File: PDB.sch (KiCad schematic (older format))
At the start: 3 parts

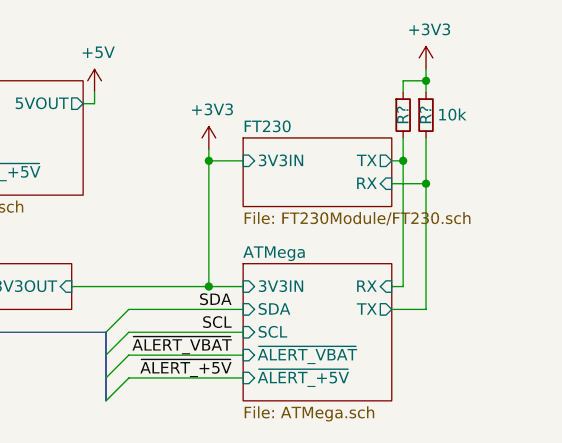
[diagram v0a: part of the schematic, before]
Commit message: add rx/tx labels
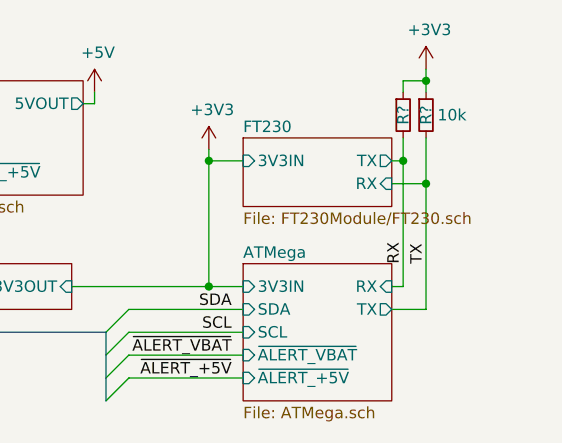
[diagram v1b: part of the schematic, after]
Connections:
- net ATMega/RX renamed RX
- net ATMega/TX renamed TX
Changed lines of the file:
@@
 Wire Wire Line
 	8700 2350 8700 2550
+Connection ~ 8700 2550
 Wire Bus Line
 	4300 2400 4300 2700
@@
 Wire Bus Line
 	7300 3200 7300 3500
-Connection ~ 8700 2550
+Text Label 8600 2900 1    50   ~ 0
+RX
+Text Label 8700 2900 1    50   ~ 0
+TX
 $EndSCHEMATC

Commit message: annotate parts
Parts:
- gave numbers to parts that had none: 3
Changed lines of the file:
@@
 P 3850 2250
 AR Path="/5C2F335D/5C33AF8D" Ref="C?"  Part="1"
-AR Path="/5C33AF8D" Ref="C?"  Part="1"
-F 0 "C?" H 3969 2525 50  0000 C CNN
+AR Path="/5C33AF8D" Ref="C1"  Part="1"
+F 0 "C1" H 3969 2525 50  0000 C CNN
 F 1 "XT-M" H 3969 2434 50  0000 C CNN
 F 2 "XT60:XT60PW" H 3850 2250 50  0001 C CNN
@@
 P 4000 2550
 AR Path="/5C2F335D/5C33AF94" Ref="#PWR?"  Part="1"
-AR Path="/5C33AF94" Ref="#PWR?"  Part="1"
-F 0 "#PWR?" H 4000 2300 50  0001 C CNN
+AR Path="/5C33AF94" Ref="#PWR01"  Part="1"
+F 0 "#PWR01" H 4000 2300 50  0001 C CNN
 F 1 "GND" H 4005 2377 50  0000 C CNN
 F 2 "" H 4000 2550 50  0001 C CNN
@@
 	3950 2200 4950 2200
 $Comp
-L power:+3V3 #PWR?
+L power:+3V3 #PWR03
 U 1 1 5C347B0C
 P 7750 2400
-F 0 "#PWR?" H 7750 2250 50  0001 C CNN
+F 0 "#PWR03" H 7750 2250 50  0001 C CNN
 F 1 "+3V3" H 7765 2573 50  0000 C CNN
 F 2 "" H 7750 2400 50  0001 C CNN
@@
 	7250 2200 7250 2150
 $Comp
-L power:+5V #PWR?
+L power:+5V #PWR02
 U 1 1 5C3483F6
 P 7250 2150
-F 0 "#PWR?" H 7250 2000 50  0001 C CNN
+F 0 "#PWR02" H 7250 2000 50  0001 C CNN
 F 1 "+5V" H 7265 2323 50  0000 C CNN
 F 2 "" H 7250 2150 50  0001 C CNN
@@
 	8700 3100 8550 3100
 $Comp
-L Device:R_Small R?
+L Device:R_Small R1
 U 1 1 5C32B264
 P 8600 2250
-F 0 "R?" V 8600 2250 50  0000 C CNN
+F 0 "R1" V 8600 2250 50  0000 C CNN
 F 1 "10k" H 8659 2205 50  0001 L CNN
 F 2 "Resistor_SMD:R_0603_1608Metric" H 8600 2250 50  0001 C CNN
@@
 $EndComp
 $Comp
-L Device:R_Small R?
+L Device:R_Small R2
 U 1 1 5C32B2AA
 P 8700 2250
-F 0 "R?" V 8700 2250 50  0000 C CNN
+F 0 "R2" V 8700 2250 50  0000 C CNN
 F 1 "10k" H 8750 2250 50  0000 L CNN
 F 2 "Resistor_SMD:R_0603_1608Metric" H 8700 2250 50  0001 C CNN
@@
 Connection ~ 8700 2100
 $Comp
-L power:+3V3 #PWR?
+L power:+3V3 #PWR04
 U 1 1 5C32C866
 P 8700 2050
-F 0 "#PWR?" H 8700 1900 50  0001 C CNN
+F 0 "#PWR04" H 8700 1900 50  0001 C CNN
 F 1 "+3V3" H 8715 2223 50  0000 C CNN
 F 2 "" H 8700 2050 50  0001 C CNN
@@
 	8700 2350 8700 2550
 Connection ~ 8700 2550
+Text Label 8600 2900 1    50   ~ 0
+RX
+Text Label 8700 2900 1    50   ~ 0
+TX
 Wire Bus Line
 	4300 2400 4300 2700
@@
 Wire Bus Line
 	7300 3200 7300 3500
-Text Label 8600 2900 1    50   ~ 0
-RX
-Text Label 8700 2900 1    50   ~ 0
-TX
 $EndSCHEMATC

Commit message: update XT60
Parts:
- C1: footprint XT60:XT60PW -> XT60:XT60PW-M
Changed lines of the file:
@@
 F 0 "C1" H 3969 2525 50  0000 C CNN
 F 1 "XT-M" H 3969 2434 50  0000 C CNN
-F 2 "XT60:XT60PW" H 3850 2250 50  0001 C CNN
+F 2 "XT60:XT60PW-M" H 3850 2250 50  0001 C CNN
 F 3 "" H 3850 2250 50  0001 C CNN
 	1    3850 2250

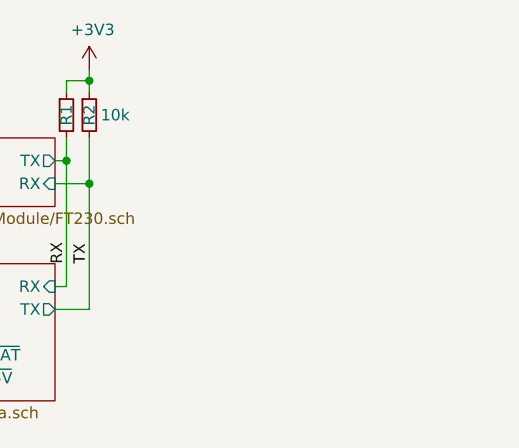
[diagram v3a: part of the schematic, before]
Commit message: add XT30 5V Out
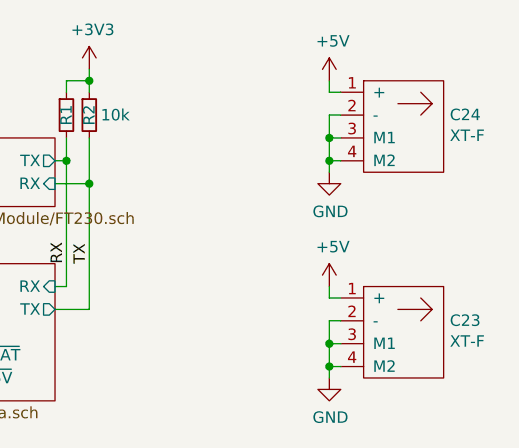
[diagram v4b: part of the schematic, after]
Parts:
- added C23, C24: XT-F, XT30:XT30PW-F, symbol amass:XT-F
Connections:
- net +5V: now also C23.1 (+), C24.1 (+)
- net GND: now also C23.2 (-), C23.3 (M1), C23.4 (M2), C24.2 (-), C24.3 (M1), C24.4 (M2)
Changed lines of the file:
@@
 F4 "3V3IN" I L 7900 2450 50
 $EndSheet
-Wire Wire Line
-	5850 2200 6550 2200
 Connection ~ 5850 2200
 Wire Wire Line
@@
 Text Label 8700 2900 1    50   ~ 0
 TX
+$Comp
+L amass:XT-F C23
+U 1 1 5C895801
+P 9900 3100
+F 0 "C23" H 10277 3051 50  0000 L CNN
+F 1 "XT-F" H 10277 2960 50  0000 L CNN
+F 2 "XT30:XT30PW-F" H 9900 3100 50  0001 C CNN
+F 3 "" H 9900 3100 50  0001 C CNN
+	1    9900 3100
+	1    0    0    -1
+$EndComp
+$Comp
+L power:+5V #PWR030
+U 1 1 5C8958C1
+P 9750 3000
+F 0 "#PWR030" H 9750 2850 50  0001 C CNN
+F 1 "+5V" H 9765 3173 50  0000 C CNN
+F 2 "" H 9750 3000 50  0001 C CNN
+F 3 "" H 9750 3000 50  0001 C CNN
+	1    9750 3000
+	1    0    0    -1
+$EndComp
+$Comp
+L power:GND #PWR?
+U 1 1 5C895918
+P 9750 3400
+AR Path="/5C2F335D/5C895918" Ref="#PWR?"  Part="1"
+AR Path="/5C895918" Ref="#PWR031"  Part="1"
+F 0 "#PWR031" H 9750 3150 50  0001 C CNN
+F 1 "GND" H 9755 3227 50  0000 C CNN
+F 2 "" H 9750 3400 50  0001 C CNN
+F 3 "" H 9750 3400 50  0001 C CNN
+	1    9750 3400
+	1    0    0    -1
+$EndComp
+Wire Wire Line
+	9750 3400 9750 3350
+Wire Wire Line
+	9750 3350 9800 3350
+Wire Wire Line
+	9750 3350 9750 3250
+Wire Wire Line
+	9750 3150 9800 3150
+Connection ~ 9750 3350
+Wire Wire Line
+	9800 3250 9750 3250
+Connection ~ 9750 3250
+Wire Wire Line
+	9750 3250 9750 3150
+Wire Wire Line
+	9800 3050 9750 3050
+Wire Wire Line
+	9750 3050 9750 3000
+$Comp
+L amass:XT-F C24
+U 1 1 5C899EE1
+P 9900 2200
+F 0 "C24" H 10277 2151 50  0000 L CNN
+F 1 "XT-F" H 10277 2060 50  0000 L CNN
+F 2 "XT30:XT30PW-F" H 9900 2200 50  0001 C CNN
+F 3 "" H 9900 2200 50  0001 C CNN
+	1    9900 2200
+	1    0    0    -1
+$EndComp
+$Comp
+L power:+5V #PWR032
+U 1 1 5C899EE7
+P 9750 2100
+F 0 "#PWR032" H 9750 1950 50  0001 C CNN
+F 1 "+5V" H 9765 2273 50  0000 C CNN
+F 2 "" H 9750 2100 50  0001 C CNN
+F 3 "" H 9750 2100 50  0001 C CNN
+	1    9750 2100
+	1    0    0    -1
+$EndComp
+$Comp
+L power:GND #PWR?
+U 1 1 5C899EED
+P 9750 2500
+AR Path="/5C2F335D/5C899EED" Ref="#PWR?"  Part="1"
+AR Path="/5C899EED" Ref="#PWR033"  Part="1"
+F 0 "#PWR033" H 9750 2250 50  0001 C CNN
+F 1 "GND" H 9755 2327 50  0000 C CNN
+F 2 "" H 9750 2500 50  0001 C CNN
+F 3 "" H 9750 2500 50  0001 C CNN
+	1    9750 2500
+	1    0    0    -1
+$EndComp
+Wire Wire Line
+	9750 2500 9750 2450
+Wire Wire Line
+	9750 2450 9800 2450
+Wire Wire Line
+	9750 2450 9750 2350
+Wire Wire Line
+	9750 2250 9800 2250
+Connection ~ 9750 2450
+Wire Wire Line
+	9800 2350 9750 2350
+Connection ~ 9750 2350
+Wire Wire Line
+	9750 2350 9750 2250
+Wire Wire Line
+	9800 2150 9750 2150
+Wire Wire Line
+	9750 2150 9750 2100
 Wire Bus Line
 	4300 2400 4300 2700
@@
 Wire Bus Line
 	7300 3200 7300 3500
+Wire Wire Line
+	5850 2200 6550 2200
 $EndSCHEMATC

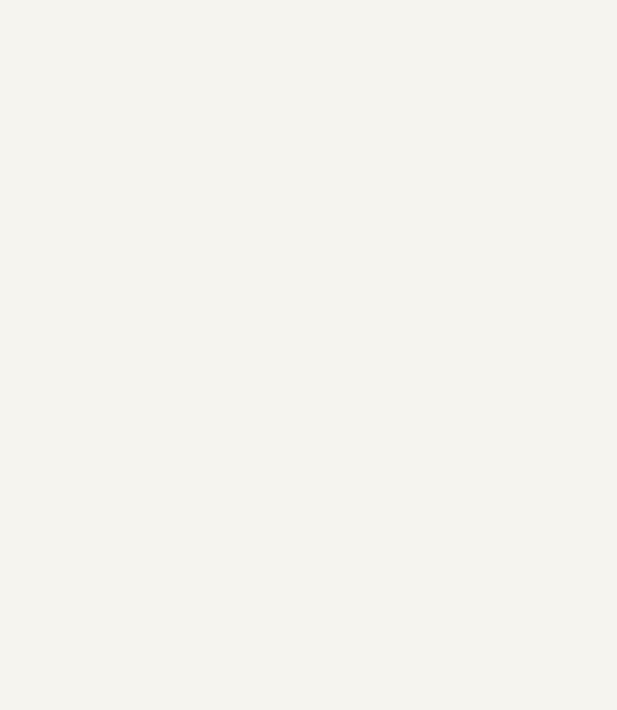
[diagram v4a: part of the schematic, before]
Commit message: USB C Power Port
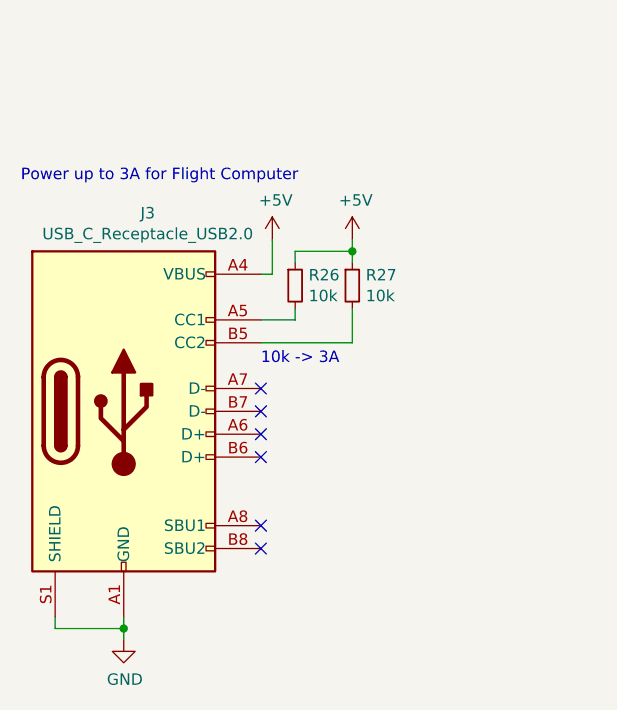
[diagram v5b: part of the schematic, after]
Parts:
- added J3: USB_C_Receptacle_USB2.0, GT-USB-7010:USB_C_Receptacle_GT-USB-7010, symbol Connector:USB_C_Receptacle_USB2.0
- added R26, R27: 10k, Resistor_SMD:R_0603_1608Metric, symbol Device:R_Small
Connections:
- net +5V: now also J3.A4 (VBUS), J3.A9 (VBUS), J3.B4 (VBUS), J3.B9 (VBUS), R26.1, R27.1
- net GND: now also J3.A1 (GND), J3.A12 (GND), J3.B1 (GND), J3.B12 (GND), J3.S1 (SHIELD)
- new net: J3.A5 (CC1), R26.2
- new net: J3.B5 (CC2), R27.2
- no-connect marks 0 -> 6
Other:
- note added: "10k -> 3A"
- note added: "Power up to 3A for Flight Computer"
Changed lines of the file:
@@
 Wire Wire Line
 	9750 2150 9750 2100
+Wire Wire Line
+	5850 2200 6550 2200
+$Comp
+L Connector:USB_C_Receptacle_USB2.0 J3
+U 1 1 5C8A8E22
+P 2200 4950
+F 0 "J3" H 2305 5817 50  0000 C CNN
+F 1 "USB_C_Receptacle_USB2.0" H 2305 5726 50  0000 C CNN
+F 2 "GT-USB-7010:USB_C_Receptacle_GT-USB-7010" H 2350 4950 50  0001 C CNN
+F 3 "https://www.usb.org/sites/default/files/documents/usb_type-c.zip" H 2350 4950 50  0001 C CNN
+	1    2200 4950
+	1    0    0    -1
+$EndComp
+$Comp
+L power:+5V #PWR035
+U 1 1 5C8A9251
+P 2850 4200
+F 0 "#PWR035" H 2850 4050 50  0001 C CNN
+F 1 "+5V" H 2865 4373 50  0000 C CNN
+F 2 "" H 2850 4200 50  0001 C CNN
+F 3 "" H 2850 4200 50  0001 C CNN
+	1    2850 4200
+	1    0    0    -1
+$EndComp
+Wire Wire Line
+	2850 4350 2800 4350
+$Comp
+L Device:R_Small R26
+U 1 1 5C8AB34A
+P 2950 4400
+F 0 "R26" H 3009 4446 50  0000 L CNN
+F 1 "10k" H 3009 4355 50  0000 L CNN
+F 2 "Resistor_SMD:R_0603_1608Metric" H 2950 4400 50  0001 C CNN
+F 3 "~" H 2950 4400 50  0001 C CNN
+	1    2950 4400
+	1    0    0    -1
+$EndComp
+$Comp
+L Device:R_Small R27
+U 1 1 5C8AB496
+P 3200 4400
+F 0 "R27" H 3259 4446 50  0000 L CNN
+F 1 "10k" H 3259 4355 50  0000 L CNN
+F 2 "Resistor_SMD:R_0603_1608Metric" H 3200 4400 50  0001 C CNN
+F 3 "~" H 3200 4400 50  0001 C CNN
+	1    3200 4400
+	1    0    0    -1
+$EndComp
+Wire Wire Line
+	2800 4550 2950 4550
+Wire Wire Line
+	2950 4550 2950 4500
+Wire Wire Line
+	2800 4650 3200 4650
+Wire Wire Line
+	3200 4650 3200 4500
+Wire Wire Line
+	2950 4300 2950 4250
+Wire Wire Line
+	3200 4300 3200 4250
+Wire Wire Line
+	3200 4250 2950 4250
+Wire Wire Line
+	2850 4200 2850 4350
+Wire Wire Line
+	3200 4250 3200 4200
+Connection ~ 3200 4250
+$Comp
+L power:+5V #PWR036
+U 1 1 5C8B41F2
+P 3200 4200
+F 0 "#PWR036" H 3200 4050 50  0001 C CNN
+F 1 "+5V" H 3215 4373 50  0000 C CNN
+F 2 "" H 3200 4200 50  0001 C CNN
+F 3 "" H 3200 4200 50  0001 C CNN
+	1    3200 4200
+	1    0    0    -1
+$EndComp
+Text Notes 2800 4750 0    50   ~ 0
+10k -> 3A
+NoConn ~ 2800 4850
+NoConn ~ 2800 4950
+NoConn ~ 2800 5050
+NoConn ~ 2800 5150
+NoConn ~ 2800 5450
+NoConn ~ 2800 5550
+$Comp
+L power:GND #PWR?
+U 1 1 5C8BB2AE
+P 2200 5950
+AR Path="/5C2F335D/5C8BB2AE" Ref="#PWR?"  Part="1"
+AR Path="/5C8BB2AE" Ref="#PWR034"  Part="1"
+F 0 "#PWR034" H 2200 5700 50  0001 C CNN
+F 1 "GND" H 2205 5777 50  0000 C CNN
+F 2 "" H 2200 5950 50  0001 C CNN
+F 3 "" H 2200 5950 50  0001 C CNN
+	1    2200 5950
+	1    0    0    -1
+$EndComp
+Wire Wire Line
+	1900 5850 1900 5900
+Wire Wire Line
+	1900 5900 2200 5900
+Wire Wire Line
+	2200 5900 2200 5850
+Wire Wire Line
+	2200 5950 2200 5900
 Wire Bus Line
 	4300 2400 4300 2700
@@
 Wire Bus Line
 	7300 3200 7300 3500
-Wire Wire Line
-	5850 2200 6550 2200
+Connection ~ 2200 5900
+Text Notes 1750 3950 0    50   ~ 0
+Power up to 3A for Flight Computer
 $EndSCHEMATC

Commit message: wip und so
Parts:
- removed C1: XT-M, XT60:XT60PW-M, symbol amass:XT-M
- removed C23, C24: XT-F, XT30:XT30PW-F, symbol amass:XT-F
- removed J3: USB_C_Receptacle_USB2.0, GT-USB-7010:USB_C_Receptacle_GT-USB-7010, symbol Connector:USB_C_Receptacle_USB2.0
- removed R26, R27: 10k, Resistor_SMD:R_0603_1608Metric, symbol Device:R_Small
- added J3, J4, J5: Conn_01x02, XT30:XT30PB-F, symbol Connector_Generic:Conn_01x02
- added J6: Conn_01x02, XT60:XT60PB-M, symbol Connector_Generic:Conn_01x02
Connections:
- net +5V: now also J3.2 (Pin_2), J4.2 (Pin_2), J5.2 (Pin_2)
- net BAT/VBATIN: now also J6.2 (Pin_2)
- net GND: now also J3.1 (Pin_1), J4.1 (Pin_1), J5.1 (Pin_1), J6.1 (Pin_1)
- no-connect marks 6 -> 0
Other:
- note removed: "10k -> 3A"
- note removed: "Power up to 3A for Flight Computer"

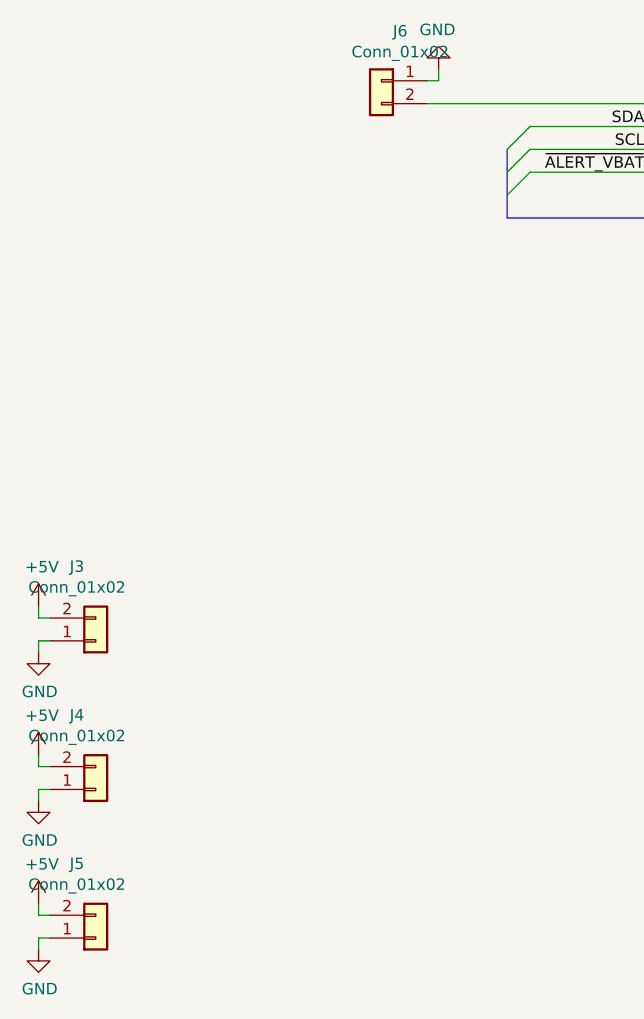
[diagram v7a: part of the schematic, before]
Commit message: LMZM23600 from kicad libs
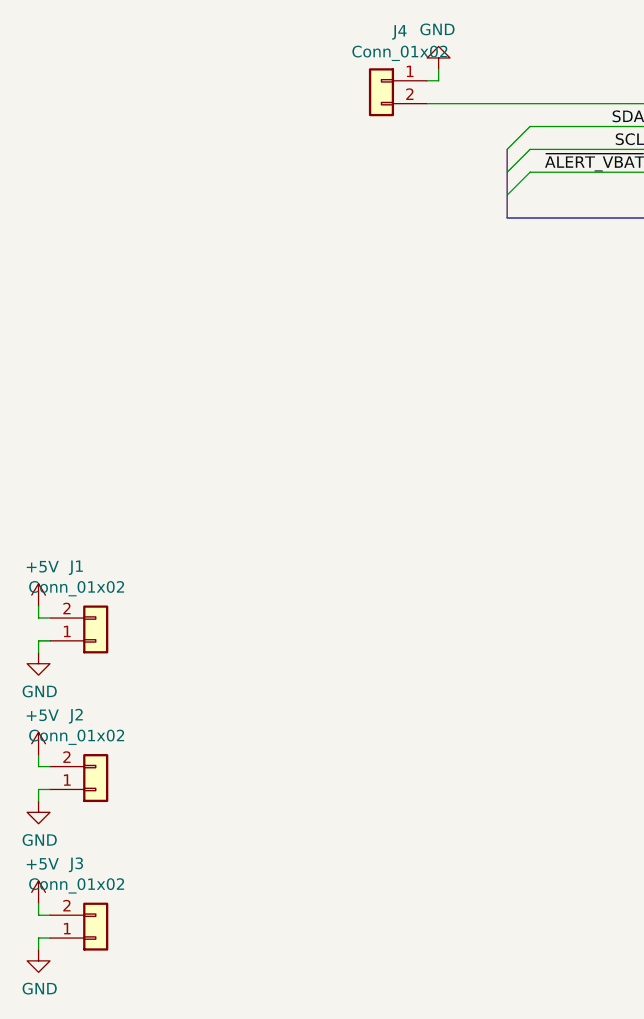
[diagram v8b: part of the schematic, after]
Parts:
- renumbered J3 to J1, J4 to J2, J5 to J3, J6 to J4
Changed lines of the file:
@@
 P 4000 2050
 AR Path="/5C2F335D/5C33AF94" Ref="#PWR?"  Part="1"
-AR Path="/5C33AF94" Ref="#PWR01"  Part="1"
-F 0 "#PWR01" H 4000 1800 50  0001 C CNN
+AR Path="/5C33AF94" Ref="#PWR07"  Part="1"
+F 0 "#PWR07" H 4000 1800 50  0001 C CNN
 F 1 "GND" H 4005 1877 50  0000 C CNN
 F 2 "" H 4000 2050 50  0001 C CNN
@@
 	3950 2200 4950 2200
 $Comp
-L power:+3V3 #PWR03
+L power:+3V3 #PWR09
 U 1 1 5C347B0C
 P 7750 2400
-F 0 "#PWR03" H 7750 2250 50  0001 C CNN
+F 0 "#PWR09" H 7750 2250 50  0001 C CNN
 F 1 "+3V3" H 7765 2573 50  0000 C CNN
 F 2 "" H 7750 2400 50  0001 C CNN
@@
 	7250 2200 7250 2150
 $Comp
-L power:+5V #PWR02
+L power:+5V #PWR08
 U 1 1 5C3483F6
 P 7250 2150
-F 0 "#PWR02" H 7250 2000 50  0001 C CNN
+F 0 "#PWR08" H 7250 2000 50  0001 C CNN
 F 1 "+5V" H 7265 2323 50  0000 C CNN
 F 2 "" H 7250 2150 50  0001 C CNN
@@
 Connection ~ 8700 2100
 $Comp
-L power:+3V3 #PWR04
+L power:+3V3 #PWR010
 U 1 1 5C32C866
 P 8700 2050
-F 0 "#PWR04" H 8700 1900 50  0001 C CNN
+F 0 "#PWR010" H 8700 1900 50  0001 C CNN
 F 1 "+3V3" H 8715 2223 50  0000 C CNN
 F 2 "" H 8700 2050 50  0001 C CNN
@@
 TX
 $Comp
-L power:+5V #PWR030
+L power:+5V #PWR03
 U 1 1 5C8958C1
 P 2250 5050
-F 0 "#PWR030" H 2250 4900 50  0001 C CNN
+F 0 "#PWR03" H 2250 4900 50  0001 C CNN
 F 1 "+5V" H 2265 5223 50  0000 C CNN
 F 2 "" H 2250 5050 50  0001 C CNN
@@
 P 2250 5250
 AR Path="/5C2F335D/5C895918" Ref="#PWR?"  Part="1"
-AR Path="/5C895918" Ref="#PWR031"  Part="1"
-F 0 "#PWR031" H 2250 5000 50  0001 C CNN
+AR Path="/5C895918" Ref="#PWR04"  Part="1"
+F 0 "#PWR04" H 2250 5000 50  0001 C CNN
 F 1 "GND" H 2255 5077 50  0000 C CNN
 F 2 "" H 2250 5250 50  0001 C CNN
@@
 	2250 5100 2250 5050
 $Comp
-L power:+5V #PWR032
+L power:+5V #PWR01
 U 1 1 5C899EE7
 P 2250 4400
-F 0 "#PWR032" H 2250 4250 50  0001 C CNN
+F 0 "#PWR01" H 2250 4250 50  0001 C CNN
 F 1 "+5V" H 2265 4573 50  0000 C CNN
 F 2 "" H 2250 4400 50  0001 C CNN
@@
 P 2250 4600
 AR Path="/5C2F335D/5C899EED" Ref="#PWR?"  Part="1"
-AR Path="/5C899EED" Ref="#PWR033"  Part="1"
-F 0 "#PWR033" H 2250 4350 50  0001 C CNN
+AR Path="/5C899EED" Ref="#PWR02"  Part="1"
+F 0 "#PWR02" H 2250 4350 50  0001 C CNN
 F 1 "GND" H 2255 4427 50  0000 C CNN
 F 2 "" H 2250 4600 50  0001 C CNN
@@
 	5850 2200 6550 2200
 $Comp
-L Connector_Generic:Conn_01x02 J4
+L Connector_Generic:Conn_01x02 J2
 U 1 1 5CAA71D1
 P 2500 5200
-F 0 "J4" H 2418 4875 50  0000 C CNN
+F 0 "J2" H 2418 4875 50  0000 C CNN
 F 1 "Conn_01x02" H 2418 4966 50  0000 C CNN
 F 2 "XT30:XT30PB-F" H 2500 5200 50  0001 C CNN
@@
 	2250 5200 2250 5250
 $Comp
-L Connector_Generic:Conn_01x02 J3
+L Connector_Generic:Conn_01x02 J1
 U 1 1 5CAA665E
 P 2500 4550
-F 0 "J3" H 2418 4225 50  0000 C CNN
+F 0 "J1" H 2418 4225 50  0000 C CNN
 F 1 "Conn_01x02" H 2418 4316 50  0000 C CNN
 F 2 "XT30:XT30PB-F" H 2500 4550 50  0001 C CNN
@@
 	2250 4600 2250 4550
 $Comp
-L power:+5V #PWR0101
+L power:+5V #PWR05
 U 1 1 5CAABE9B
 P 2250 5700
-F 0 "#PWR0101" H 2250 5550 50  0001 C CNN
+F 0 "#PWR05" H 2250 5550 50  0001 C CNN
 F 1 "+5V" H 2265 5873 50  0000 C CNN
 F 2 "" H 2250 5700 50  0001 C CNN
@@
 P 2250 5900
 AR Path="/5C2F335D/5CAABEA5" Ref="#PWR?"  Part="1"
-AR Path="/5CAABEA5" Ref="#PWR0102"  Part="1"
-F 0 "#PWR0102" H 2250 5650 50  0001 C CNN
+AR Path="/5CAABEA5" Ref="#PWR06"  Part="1"
+F 0 "#PWR06" H 2250 5650 50  0001 C CNN
 F 1 "GND" H 2255 5727 50  0000 C CNN
 F 2 "" H 2250 5900 50  0001 C CNN
@@
 	2250 5750 2250 5700
 $Comp
-L Connector_Generic:Conn_01x02 J5
+L Connector_Generic:Conn_01x02 J3
 U 1 1 5CAABEB2
 P 2500 5850
-F 0 "J5" H 2418 5525 50  0000 C CNN
+F 0 "J3" H 2418 5525 50  0000 C CNN
 F 1 "Conn_01x02" H 2418 5616 50  0000 C CNN
 F 2 "XT30:XT30PB-F" H 2500 5850 50  0001 C CNN
@@
 	4000 2100 4000 2050
 $Comp
-L Connector_Generic:Conn_01x02 J6
+L Connector_Generic:Conn_01x02 J4
 U 1 1 5CA415F9
 P 3750 2100
-F 0 "J6" H 3668 2317 50  0000 C CNN
+F 0 "J4" H 3668 2317 50  0000 C CNN
 F 1 "Conn_01x02" H 3668 2226 50  0000 C CNN
 F 2 "XT60:XT60PB-M" H 3750 2100 50  0001 C CNN
